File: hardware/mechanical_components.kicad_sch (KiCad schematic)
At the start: 9 parts, among them J500 Conn_01x01_Socket, J501 Conn_01x01_Socket

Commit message: Routing close to completion. Pending review.
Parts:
- added H400 (x4): ~, MountingHole:MountingHole_2.2mm_M2_ISO7380_Pad_TopOnly, symbol Mechanical:MountingHole_Pad
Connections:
- net GND: now also H400.1, H400.1, H400.1, H400.1
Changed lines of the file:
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@@
   (junction (at 45.085 38.735) (diameter 0) (color 0 0 0 0)
   )
+  (junction (at 38.1 64.135) (diameter 0) (color 0 0 0 0)
+  )
   (junction (at 93.98 38.1) (diameter 0) (color 0 0 0 0)
   )
+  (junction (at 45.085 64.135) (diameter 0) (color 0 0 0 0)
+  )
   (junction (at 31.75 38.735) (diameter 0) (color 0 0 0 0)
   )
+  (junction (at 31.75 64.135) (diameter 0) (color 0 0 0 0)
+  )
   (junction (at 106.68 38.1) (diameter 0) (color 0 0 0 0)
   )
@@
     (stroke (width 0) (type default))
   )
+  (wire (pts (xy 38.1 64.135) (xy 45.085 64.135))
+    (stroke (width 0) (type default))
+  )
   (wire (pts (xy 125.73 40.64) (xy 111.76 40.64))
     (stroke (width 0) (type default))
@@
     (stroke (width 0) (type default))
   )
+  (wire (pts (xy 25.4 64.135) (xy 31.75 64.135))
+    (stroke (width 0) (type default))
+  )
   (wire (pts (xy 81.28 38.1) (xy 93.98 38.1))
     (stroke (width 0) (type default))
@@
     (stroke (width 0) (type default))
   )
+  (wire (pts (xy 45.085 64.135) (xy 45.085 68.58))
+    (stroke (width 0) (type default))
+  )
+  (wire (pts (xy 45.085 60.96) (xy 45.085 64.135))
+    (stroke (width 0) (type default))
+  )
   (wire (pts (xy 96.52 40.64) (xy 111.76 40.64))
     (stroke (width 0) (type default))
@@
     (stroke (width 0) (type default))
   )
+  (wire (pts (xy 31.75 60.96) (xy 31.75 64.135))
+    (stroke (width 0) (type default))
+  )
   (wire (pts (xy 125.73 31.75) (xy 125.73 40.64))
     (stroke (width 0) (type default))
@@
     (stroke (width 0) (type default))
   )
+  (wire (pts (xy 38.1 60.96) (xy 38.1 64.135))
+    (stroke (width 0) (type default))
+  )
   (wire (pts (xy 38.1 38.735) (xy 45.085 38.735))
     (stroke (width 0) (type default))
   )
+  (wire (pts (xy 25.4 60.96) (xy 25.4 64.135))
+    (stroke (width 0) (type default))
+  )
   (wire (pts (xy 111.76 33.02) (xy 111.76 40.64))
     (stroke (width 0) (type default))
@@
   )
   (wire (pts (xy 25.4 38.735) (xy 31.75 38.735))
+    (stroke (width 0) (type default))
+  )
+  (wire (pts (xy 31.75 64.135) (xy 38.1 64.135))
     (stroke (width 0) (type default))
   )
@@
     )
   )
+  (symbol (lib_id "power:GND") (at 45.085 68.58 0) (unit 1)
+    (in_bom yes) (on_board yes) (dnp no) (fields_autoplaced)
+    (property "Reference" "#PWR06" (at 45.085 74.93 0)
+      (effects (font (size 1.27 1.27)) hide)
+    )
+    (property "Value" "GND" (at 45.085 73.025 0)
+      (effects (font (size 1.27 1.27)))
+    )
+    (property "Footprint" "" (at 45.085 68.58 0)
+      (effects (font (size 1.27 1.27)) hide)
+    )
+    (property "Datasheet" "" (at 45.085 68.58 0)
+      (effects (font (size 1.27 1.27)) hide)
+    )
+    (pin "1")
+    (instances
+      (project "business_card"
+        (path "/51aec97f-d68d-4a03-8084-46676bd22396"
+          (reference "#PWR06") (unit 1)
+        )
+      )
+      (project "current_sink_dev"
+        (path "/695b42ec-77e0-4be3-bf4d-1fc5cfcb9ef1/0c6362b3-70d1-4005-b89b-9ee91ccddbc7"
+          (reference "#PWR0413") (unit 1)
+        )
+        (path "/695b42ec-77e0-4be3-bf4d-1fc5cfcb9ef1/4d701625-90e5-43d0-9a70-5f605f6518f8"
+          (reference "#PWR0513") (unit 1)
+        )
+      )
+    )
+  )
   (symbol (lib_id "Connector:Conn_01x01_Socket") (at 125.73 26.67 90) (unit 1)
     (in_bom yes) (on_board yes) (dnp no)
@@
     )
   )
+  (symbol (lib_id "Mechanical:MountingHole_Pad") (at 25.4 58.42 0) (unit 1)
+    (in_bom yes) (on_board yes) (dnp no)
+    (property "Reference" "H400" (at 22.86 53.34 0)
+      (effects (font (size 1.27 1.27)) (justify left))
+    )
+    (property "Value" "~" (at 28.575 59.055 0)
+      (effects (font (size 1.27 1.27)) (justify left))
+    )
+    (property "Footprint" "MountingHole:MountingHole_2.2mm_M2_ISO7380_Pad_TopOnly" (at 25.4 58.42 0)
+      (effects (font (size 1.27 1.27)) hide)
+    )
+    (property "Datasheet" "~" (at 25.4 58.42 0)
+      (effects (font (size 1.27 1.27)) hide)
+    )
+    (pin "1")
+    (instances
+      (project "current_sink_dev"
+        (path "/695b42ec-77e0-4be3-bf4d-1fc5cfcb9ef1/0c6362b3-70d1-4005-b89b-9ee91ccddbc7"
+          (reference "H400") (unit 1)
+        )
+        (path "/695b42ec-77e0-4be3-bf4d-1fc5cfcb9ef1/4d701625-90e5-43d0-9a70-5f605f6518f8"
+          (reference "H506") (unit 1)
+        )
+      )
+    )
+  )
   (symbol (lib_id "Mechanical:MountingHole_Pad") (at 106.68 30.48 0) (unit 1)
     (in_bom yes) (on_board yes) (dnp no)
@@
     )
   )
+  (symbol (lib_id "Mechanical:MountingHole_Pad") (at 45.085 58.42 0) (unit 1)
+    (in_bom yes) (on_board yes) (dnp no)
+    (property "Reference" "H400" (at 42.545 53.34 0)
+      (effects (font (size 1.27 1.27)) (justify left))
+    )
+    (property "Value" "~" (at 48.26 59.055 0)
+      (effects (font (size 1.27 1.27)) (justify left))
+    )
+    (property "Footprint" "MountingHole:MountingHole_2.2mm_M2_ISO7380_Pad_TopOnly" (at 45.085 58.42 0)
+      (effects (font (size 1.27 1.27)) hide)
+    )
+    (property "Datasheet" "~" (at 45.085 58.42 0)
+      (effects (font (size 1.27 1.27)) hide)
+    )
+    (pin "1")
+    (instances
+      (project "current_sink_dev"
+        (path "/695b42ec-77e0-4be3-bf4d-1fc5cfcb9ef1/0c6362b3-70d1-4005-b89b-9ee91ccddbc7"
+          (reference "H400") (unit 1)
+        )
+        (path "/695b42ec-77e0-4be3-bf4d-1fc5cfcb9ef1/4d701625-90e5-43d0-9a70-5f605f6518f8"
+          (reference "H509") (unit 1)
+        )
+      )
+    )
+  )
   (symbol (lib_id "Mechanical:MountingHole_Pad") (at 38.1 33.02 0) (unit 1)
     (in_bom yes) (on_board yes) (dnp no)
@@
         )
       )
+    )
+  )
+  (symbol (lib_id "Mechanical:MountingHole_Pad") (at 31.75 58.42 0) (unit 1)
+    (in_bom yes) (on_board yes) (dnp no)
+    (property "Reference" "H400" (at 29.21 53.34 0)
+      (effects (font (size 1.27 1.27)) (justify left))
+    )
+    (property "Value" "~" (at 34.925 59.055 0)
+      (effects (font (size 1.27 1.27)) (justify left))
+    )
+    (property "Footprint" "MountingHole:MountingHole_2.2mm_M2_ISO7380_Pad_TopOnly" (at 31.75 58.42 0)
+      (effects (font (size 1.27 1.27)) hide)
+    )
+    (property "Datasheet" "~" (at 31.75 58.42 0)
+      (effects (font (size 1.27 1.27)) hide)
+    )
+    (pin "1")
+    (instances
+      (project "current_sink_dev"
+        (path "/695b42ec-77e0-4be3-bf4d-1fc5cfcb9ef1/0c6362b3-70d1-4005-b89b-9ee91ccddbc7"
+          (reference "H400") (unit 1)
+        )
+        (path "/695b42ec-77e0-4be3-bf4d-1fc5cfcb9ef1/4d701625-90e5-43d0-9a70-5f605f6518f8"
+          (reference "H507") (unit 1)
+        )
+      )
+    )
+  )
+  (symbol (lib_id "Mechanical:MountingHole_Pad") (at 38.1 58.42 0) (unit 1)
+    (in_bom yes) (on_board yes) (dnp no)
+    (property "Reference" "H400" (at 35.56 53.34 0)
+      (effects (font (size 1.27 1.27)) (justify left))
+    )
+    (property "Value" "~" (at 41.275 59.055 0)
+      (effects (font (size 1.27 1.27)) (justify left))
+    )
+    (property "Footprint" "MountingHole:MountingHole_2.2mm_M2_ISO7380_Pad_TopOnly" (at 38.1 58.42 0)
+      (effects (font (size 1.27 1.27)) hide)
+    )
+    (property "Datasheet" "~" (at 38.1 58.42 0)
+      (effects (font (size 1.27 1.27)) hide)
+    )
+    (pin "1")
+    (instances
+      (project "current_sink_dev"
+        (path "/695b42ec-77e0-4be3-bf4d-1fc5cfcb9ef1/0c6362b3-70d1-4005-b89b-9ee91ccddbc7"
+          (reference "H400") (unit 1)
+        )
+        (path "/695b42ec-77e0-4be3-bf4d-1fc5cfcb9ef1/4d701625-90e5-43d0-9a70-5f605f6518f8"
+          (reference "H508") (unit 1)
+        )
+      )

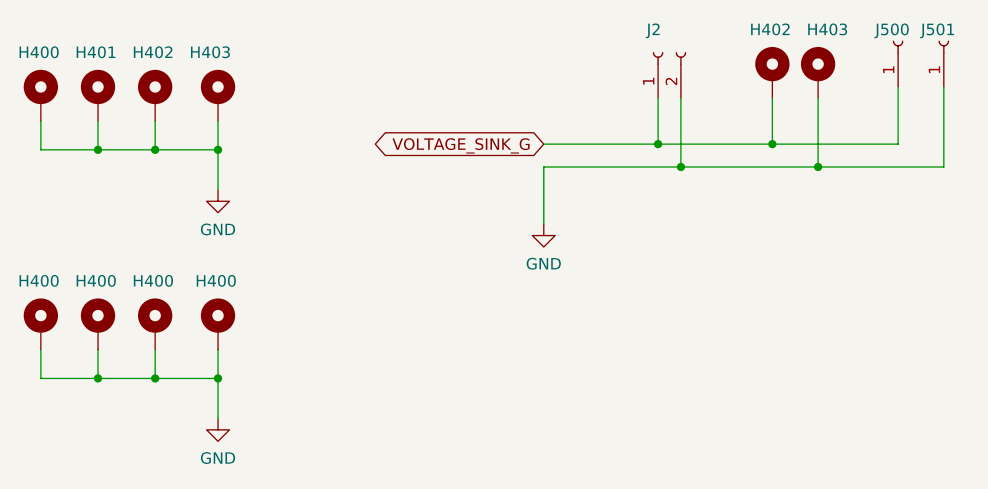
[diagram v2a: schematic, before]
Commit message: Added some doucmentation to MCP driver
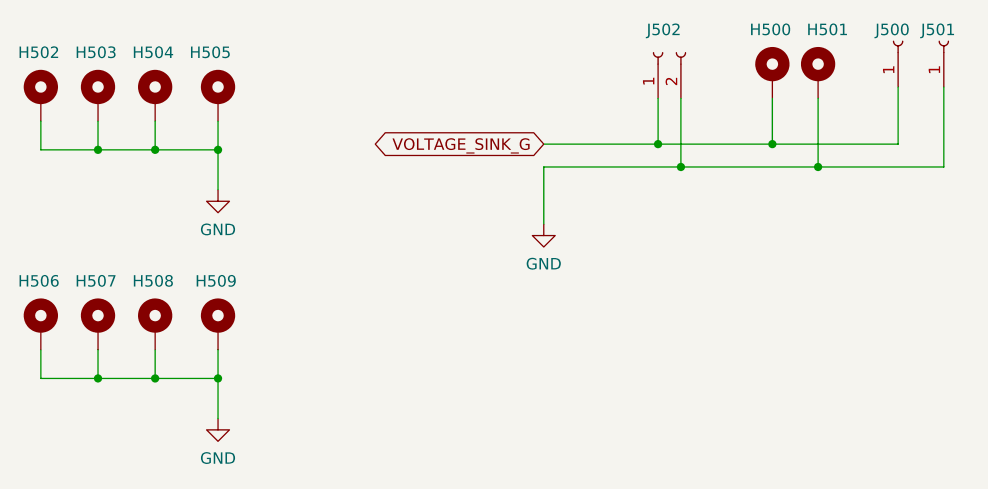
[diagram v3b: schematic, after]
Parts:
- renumbered H402 to H500, H403 to H501, H400 to H502, H401 to H503, H402 to H504, H403 to H505, H400 to H506, H400 to H507, H400 to H508, H400 to H509, J2 to J502
